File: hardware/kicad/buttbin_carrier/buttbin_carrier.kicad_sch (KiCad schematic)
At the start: 31 parts, among them J1 USB-C 6P, J2 Akku, J3 Stempel, J4 SWS/UART, Q1 FS8205, U1 TP4054, U2 DW01A, U3 XC6206P332MR, U4 TB-03F-AT_Mesh

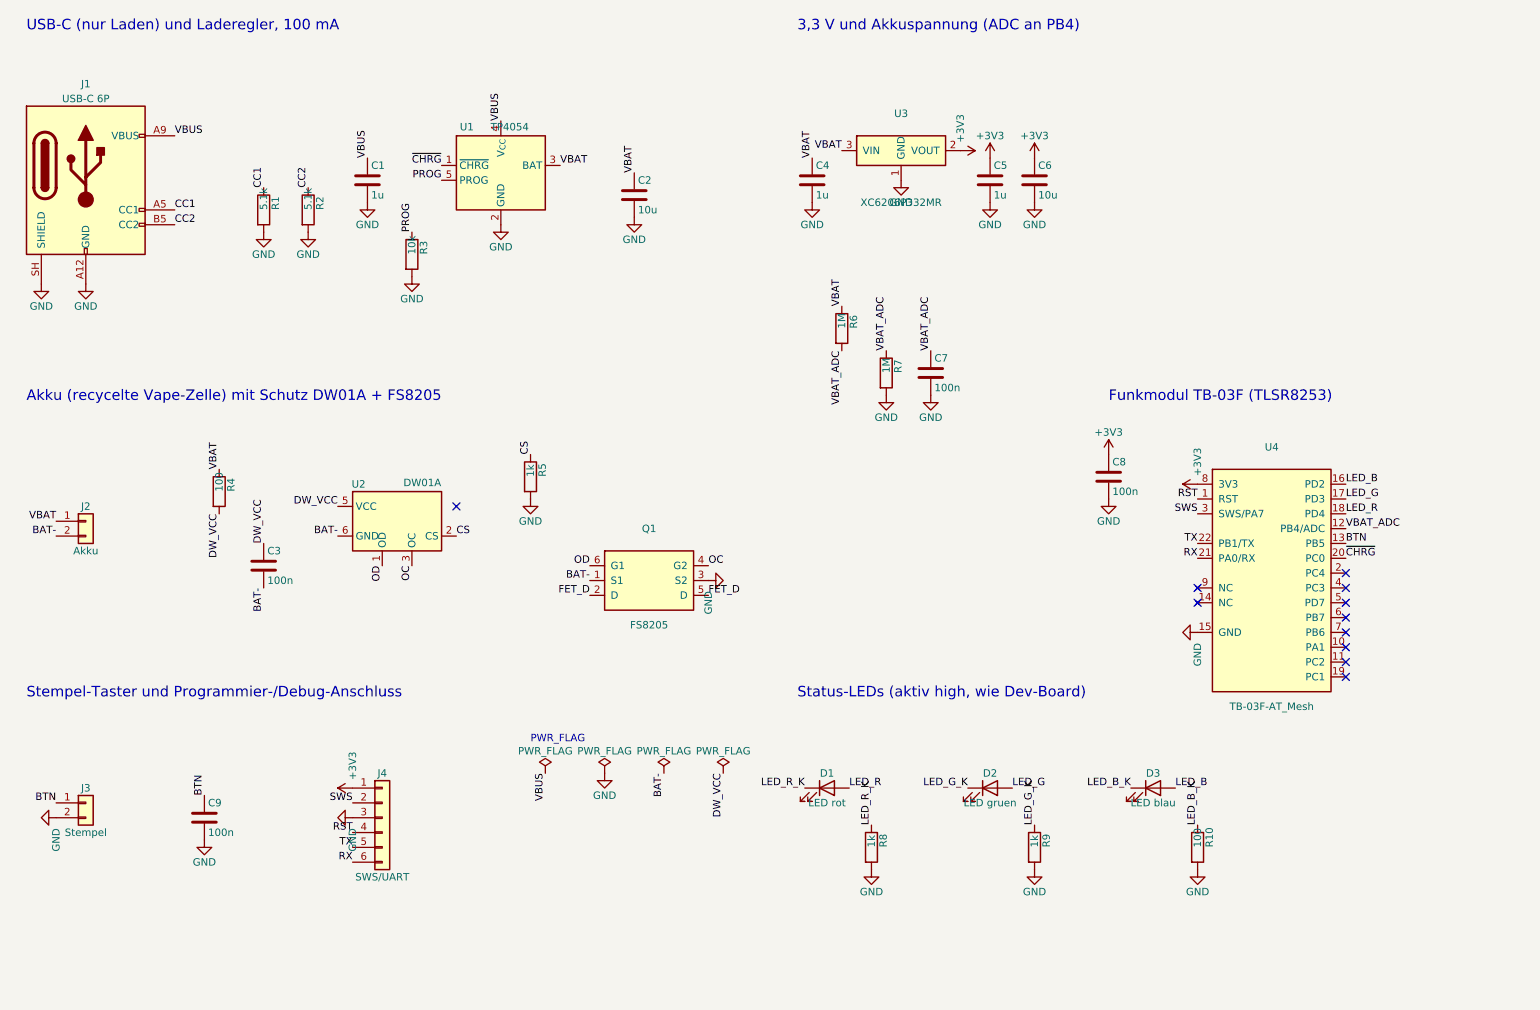
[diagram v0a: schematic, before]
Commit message: Butt Bin carrier board: schematic rev 0.3
Review feedback from Karl-Werner Riedel:
- No DW01/FS8205 and no PTC: TP4054 prevents overcharge, the firmware
  prevents deep discharge by releasing HOLD; a board fuse would not protect
  the most likely short (the cell leads) anyway
- TPS7A0333 LDO (200 nA) with enable = VBUS OR HOLD OR plunger
  (three BAT54WS); external 1M pulldown, because the internal smart pulldown
  disconnects after start-up; 1 uF keeps EN high until the firmware sets HOLD
- Plunger now switches to VBAT: first press powers the device up,
  PB5 reads it through 100k (active high)
- Battery divider 1M/1M (about 2 uA); charge LED on TP4054 CHRG
- Smaller: 0402 passives, solder pads instead of connectors
- Readable layout: real wires inside each block, labels only between blocks

Co-Authored-By: Claude Opus 5.5 <noreply@anthropic.com>
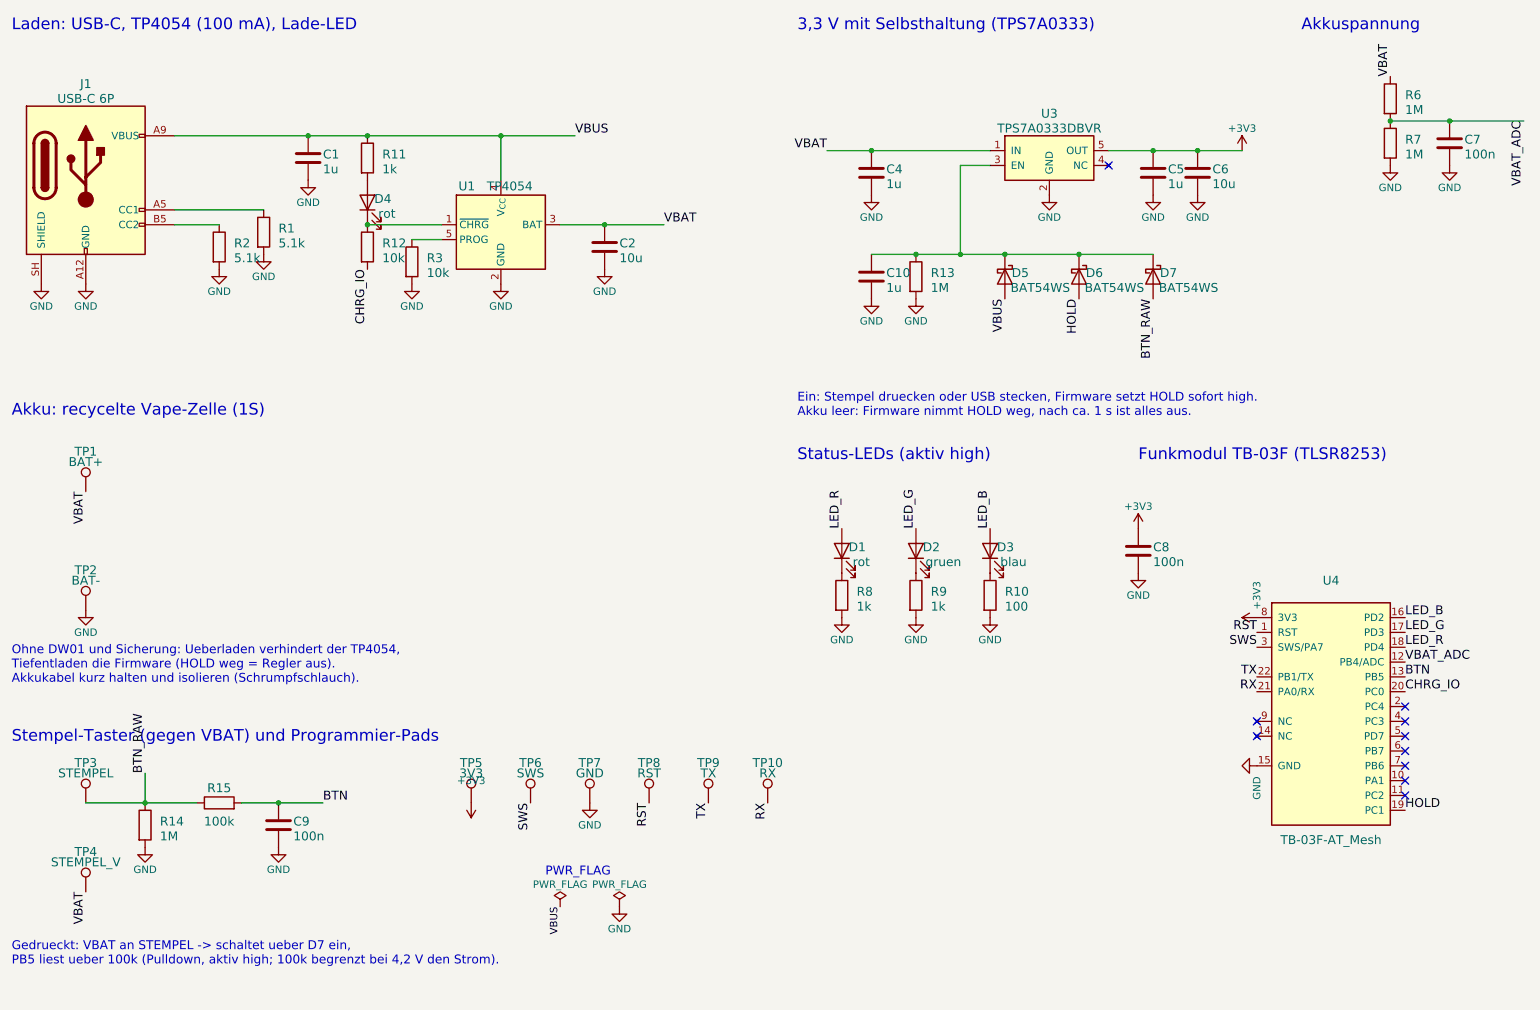
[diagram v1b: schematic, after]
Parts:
- removed C3: 100n, Capacitor_SMD:C_0603_1608Metric, symbol Device:C
- removed J2: Akku, Connector_JST:JST_PH_S2B-PH-K_1x02_P2.00mm_Horizontal, symbol Connector_Generic:Conn_01x02
- removed J3: Stempel, Connector_PinHeader_2.54mm:PinHeader_1x02_P2.54mm_Vertical, symbol Connector_Generic:Conn_01x02
- removed J4: SWS/UART, Connector_PinHeader_2.54mm:PinHeader_1x06_P2.54mm_Vertical, symbol Connector_Generic:Conn_01x06
- removed Q1: FS8205, Package_TO_SOT_SMD:SOT-23-6, symbol ButtBin:FS8205
- removed R4: 100, Resistor_SMD:R_0603_1608Metric, symbol Device:R
- removed R5: 1k, Resistor_SMD:R_0603_1608Metric, symbol Device:R
- removed U2: DW01A, Package_TO_SOT_SMD:SOT-23-6, symbol Battery_Management:DW01A
- removed U3: XC6206P332MR, Package_TO_SOT_SMD:SOT-23-3, symbol ButtBin:XC6206P332MR
- added C10: 1u, Capacitor_SMD:C_0402_1005Metric, symbol Device:C
- added D4: rot, LED_SMD:LED_0603_1608Metric, symbol Device:LED
- added D5, D6, D7: BAT54WS, Diode_SMD:D_SOD-323, symbol Device:D_Schottky
- added R11: 1k, Resistor_SMD:R_0402_1005Metric, symbol Device:R
- added R12: 10k, Resistor_SMD:R_0402_1005Metric, symbol Device:R
- added R13, R14: 1M, Resistor_SMD:R_0402_1005Metric, symbol Device:R
- added R15: 100k, Resistor_SMD:R_0402_1005Metric, symbol Device:R
- added TP1: BAT+, TestPoint:TestPoint_Pad_2.0x2.0mm, symbol Connector:TestPoint
- added TP10: RX, TestPoint:TestPoint_Pad_1.0x1.0mm, symbol Connector:TestPoint
- added TP2: BAT-, TestPoint:TestPoint_Pad_2.0x2.0mm, symbol Connector:TestPoint
- added TP3: STEMPEL, TestPoint:TestPoint_Pad_1.0x1.0mm, symbol Connector:TestPoint
- added TP4: STEMPEL_V, TestPoint:TestPoint_Pad_1.0x1.0mm, symbol Connector:TestPoint
- added TP5: 3V3, TestPoint:TestPoint_Pad_1.0x1.0mm, symbol Connector:TestPoint
- added TP6: SWS, TestPoint:TestPoint_Pad_1.0x1.0mm, symbol Connector:TestPoint
- added TP7: GND, TestPoint:TestPoint_Pad_1.0x1.0mm, symbol Connector:TestPoint
- added TP8: RST, TestPoint:TestPoint_Pad_1.0x1.0mm, symbol Connector:TestPoint
- added TP9: TX, TestPoint:TestPoint_Pad_1.0x1.0mm, symbol Connector:TestPoint
- added U3: TPS7A0333DBVR, Package_TO_SOT_SMD:SOT-23-5, symbol ButtBin:TPS7A0333DBV
- C1, C4, C5: footprint Capacitor_SMD:C_0603_1608Metric -> Capacitor_SMD:C_0402_1005Metric; LCSC C15849 -> C52923
- C2, C6: footprint Capacitor_SMD:C_0603_1608Metric -> Capacitor_SMD:C_0402_1005Metric; LCSC C19702 -> C15525
- C7, C8, C9: footprint Capacitor_SMD:C_0603_1608Metric -> Capacitor_SMD:C_0402_1005Metric; LCSC C14663 -> C1525
- D1: value LED rot -> rot
- D2: value LED gruen -> gruen
- D3: value LED blau -> blau
- R1, R2: footprint Resistor_SMD:R_0603_1608Metric -> Resistor_SMD:R_0402_1005Metric; LCSC C23186 -> C25905
- R10: footprint Resistor_SMD:R_0603_1608Metric -> Resistor_SMD:R_0402_1005Metric; LCSC C22775 -> C25076
- R3: footprint Resistor_SMD:R_0603_1608Metric -> Resistor_SMD:R_0402_1005Metric; LCSC C25804 -> C25744
- R6, R7: footprint Resistor_SMD:R_0603_1608Metric -> Resistor_SMD:R_0402_1005Metric; LCSC C22935 -> C26083
- R8, R9: footprint Resistor_SMD:R_0603_1608Metric -> Resistor_SMD:R_0402_1005Metric; LCSC C21190 -> C11702
- U4: Hinweis Antenne ueber Platinenrand, keine Metallteile daneben -> Antenne ueber Platinenrand, im Griff nur Kunststoff darueber
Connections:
- net +3V3: now also TP5.1, U3.5 (OUT)
- net BTN: now also R15.2
- net GND: now also C10.2, R13.2, R14.2, TP2.1, TP7.1, U3.2 (GND)
- net RST: now also TP8.1
- net RX: now also TP10.1
- net SWS: now also TP6.1
- net TX: now also TP9.1
- net VBAT: now also TP1.1, TP4.1, U3.1 (IN)
- net VBUS: now also D5.2 (A), R11.1
- net HOLD: now reaches U4.19 (PC1)
- net HOLD: now also D6.2 (A)
- net CC1: no longer names the net of J1.A5 (CC1), R1.1
- net CC2: no longer names the net of J1.B5 (CC2), R2.1
- net LED_B_K: no longer names the net of D3.1 (K), R10.1
- net LED_G_K: no longer names the net of D2.1 (K), R9.1
- net LED_R_K: no longer names the net of D1.1 (K), R8.1
- net PROG: no longer names the net of R3.1, U1.5 (PROG)
- net ~{CHRG}: no longer names the net of U1.1 (~{CHRG})
- net ~{CHRG}: now also D4.1 (K), R12.1; no longer U4.20 (PC0)
- new net: C10.1, D5.1 (K), D6.1 (K), D7.1 (K), R13.1, U3.3 (EN)
- new net: D4.2 (A), R11.2
- new net BTN_RAW: D7.2 (A), R14.1, R15.1, TP3.1
- new net CHRG_IO: R12.2, U4.20 (PC0)
- no-connect marks 11 -> 10
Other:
- note added: "3,3 V mit Selbsthaltung (TPS7A0333)"
- note added: "Akku: recycelte Vape-Zelle (1S)"
- note added: "Akkuspannung"
- note added: "Ein: Stempel druecken oder USB stecken, Firmware setzt HOLD sofort high. Akku leer: Firmware nimmt HOLD weg, nach ca. 1 s ist alles aus."
- note added: "Gedrueckt: VBAT an STEMPEL -> schaltet ueber D7 ein, PB5 liest ueber 100k (Pulldown, aktiv high; 100k begrenzt bei 4,2 V den Strom)."
- note added: "Laden: USB-C, TP4054 (100 mA), Lade-LED"
- note added: "Ohne DW01 und Sicherung: Ueberladen verhindert der TP4054, Tiefentladen die Firmware (HOLD weg = Regler aus). Akkukabel kurz halten und isolieren (Schrumpfschlauch)."
- note added: "Status-LEDs (aktiv high)"
- note added: "Stempel-Taster (gegen VBAT) und Programmier-Pads"
- note removed: "3,3 V und Akkuspannung (ADC an PB4)"
- note removed: "Akku (recycelte Vape-Zelle) mit Schutz DW01A + FS8205"
- note removed: "Status-LEDs (aktiv high, wie Dev-Board)"
- note removed: "Stempel-Taster und Programmier-/Debug-Anschluss"
- note removed: "USB-C (nur Laden) und Laderegler, 100 mA"

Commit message: Butt Bin carrier board: TVS diode on VBUS
5 V unidirectional TVS (CDSOD323-T05, SOD-323) right behind the USB-C
socket against overshoot when plugging in (TP4054 VCC max 10 V) and ESD.

Co-Authored-By: Claude Opus 5.5 <noreply@anthropic.com>
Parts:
- added D8: TVS 5V, Diode_SMD:D_SOD-323, symbol Device:D_Zener
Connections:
- net GND: now also D8.2 (A)
- net VBUS: now also D8.1 (K)
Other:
- note added: "Laden: USB-C mit TVS, TP4054 (100 mA), Lade-LED"
- note removed: "Laden: USB-C, TP4054 (100 mA), Lade-LED"

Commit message: Butt Bin carrier board: schematic rev 0.4 with TP4056
- TP4056 (ESOP-8) instead of TP4054: red LED while charging (CHRG),
  green LED when full (STDBY), both powered from USB only; STDBY also to
  PC4 through 10k so the firmware knows "full"
- NTC input: 6.2k from VCC plus a 10k B3950 NTC on the cell to BAT-,
  charging only between about 6 and 44 °C (window 45..80 % of VCC);
  without NTC bridge the NTC and BAT- pads
- PROG 10k = about 110 mA; exposed pad to GND

Co-Authored-By: Claude Opus 5.5 <noreply@anthropic.com>
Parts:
- removed U1: TP4054, Package_TO_SOT_SMD:SOT-23-5, symbol Battery_Management:LTC4054ES5-4.2
- added D9: gruen, LED_SMD:LED_0603_1608Metric, symbol Device:LED
- added R16: 6.2k, Resistor_SMD:R_0402_1005Metric, symbol Device:R
- added R17: 1k, Resistor_SMD:R_0402_1005Metric, symbol Device:R
- added R18: 10k, Resistor_SMD:R_0402_1005Metric, symbol Device:R
- added TP11: NTC, TestPoint:TestPoint_Pad_1.0x1.0mm, symbol Connector:TestPoint
- added U1: TP4056, Package_SO:SOIC-8-1EP_3.9x4.9mm_P1.27mm_EP2.29x3mm, symbol ButtBin:TP4056
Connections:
- net GND: now also U1.3 (GND), U1.9 (EP)
- net VBAT: now also U1.5 (BAT)
- net VBUS: now also R16.1, R17.1, U1.4 (VCC), U1.8 (CE)
- net STDBY_IO: now reaches U4.2 (PC4)
- net STDBY_IO: now also R18.2
- net ~{CHRG}: now reaches D4.1 (K), R12.1
- net ~{CHRG}: now also U1.7 (~{CHRG})
- net at R3.1: now also U1.2 (PROG)
- new net: D9.2 (A), R17.2
- new net NTC: R16.2, TP11.1, U1.1 (TEMP)
- new net ~{STDBY}: D9.1 (K), R18.1, U1.6 (~{STDBY})
- no-connect marks 10 -> 9
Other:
- note added: "Laden: USB-C mit TVS, TP4056 (ca. 110 mA), LEDs rot/gruen, NTC"
- note added: "Ohne DW01 und Sicherung: Ueberladen verhindert der TP4056, Tiefentladen die Firmware (HOLD weg = Regler aus). Akkukabel kurz halten und isolieren (Schrumpfschlauch). NTC zwischen NTC und BAT-; ohne NTC die Pads NTC und BAT- bruecken."
- note removed: "Laden: USB-C mit TVS, TP4054 (100 mA), Lade-LED"
- note removed: "Ohne DW01 und Sicherung: Ueberladen verhindert der TP4054, Tiefentladen die Firmware (HOLD weg = Regler aus). Akkukabel kurz halten und isolieren (Schrumpfschlauch)."
